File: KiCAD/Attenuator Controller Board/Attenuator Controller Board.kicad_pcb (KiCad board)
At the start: 2 copper layers, 100 x 70 mm, 33 parts, among them J1 Barrel_Jack_Switch, J2 Conn_Coaxial, J3 Conn_Coaxial, J4 Conn_01x24_Female, J5 DSub_15_HD, J6 DSub9, J7 DSub9, J8 DSub9, J9 Conn_01x24_Female, U1 ADM3307EARUZ, U2 ZXMHC3A01T8TA, U3 Teensy3.5

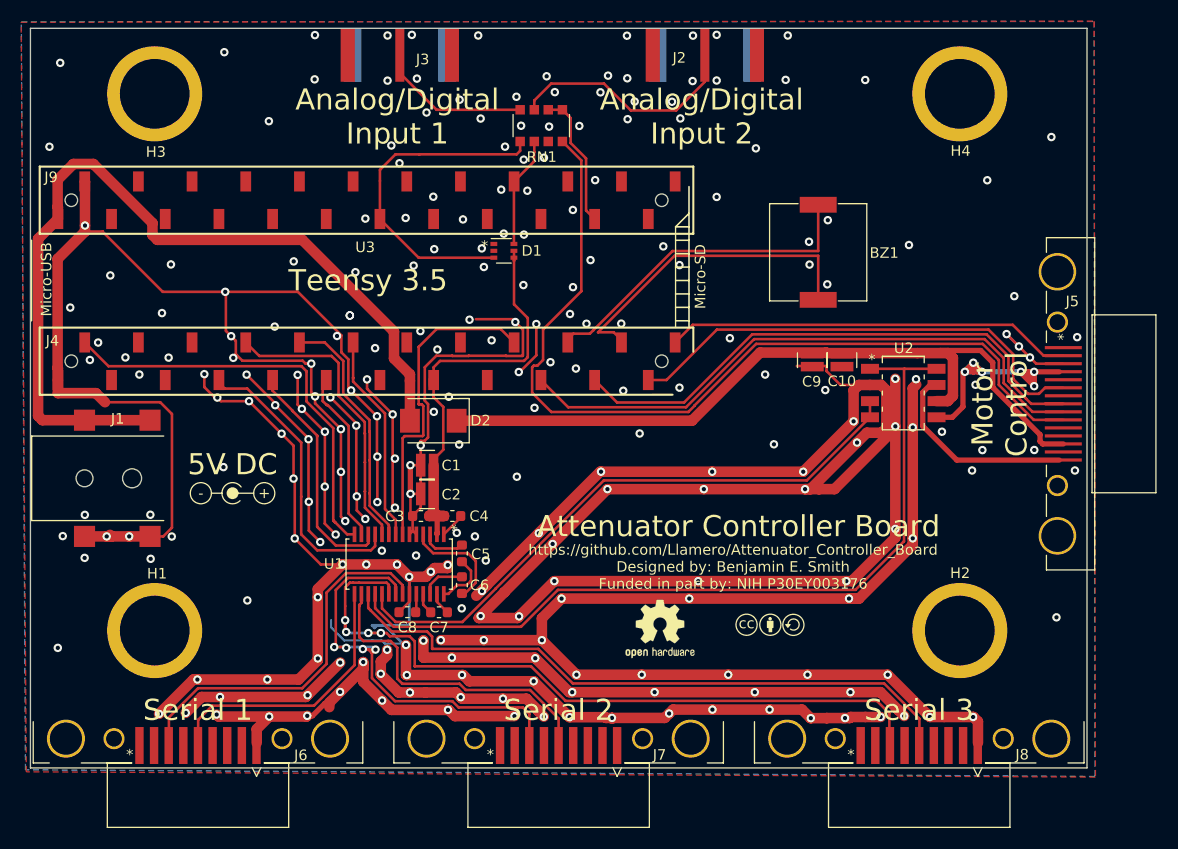
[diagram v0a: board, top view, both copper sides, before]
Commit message: Re-order annotation - add 0.1µF bypass to bypass H-bridge
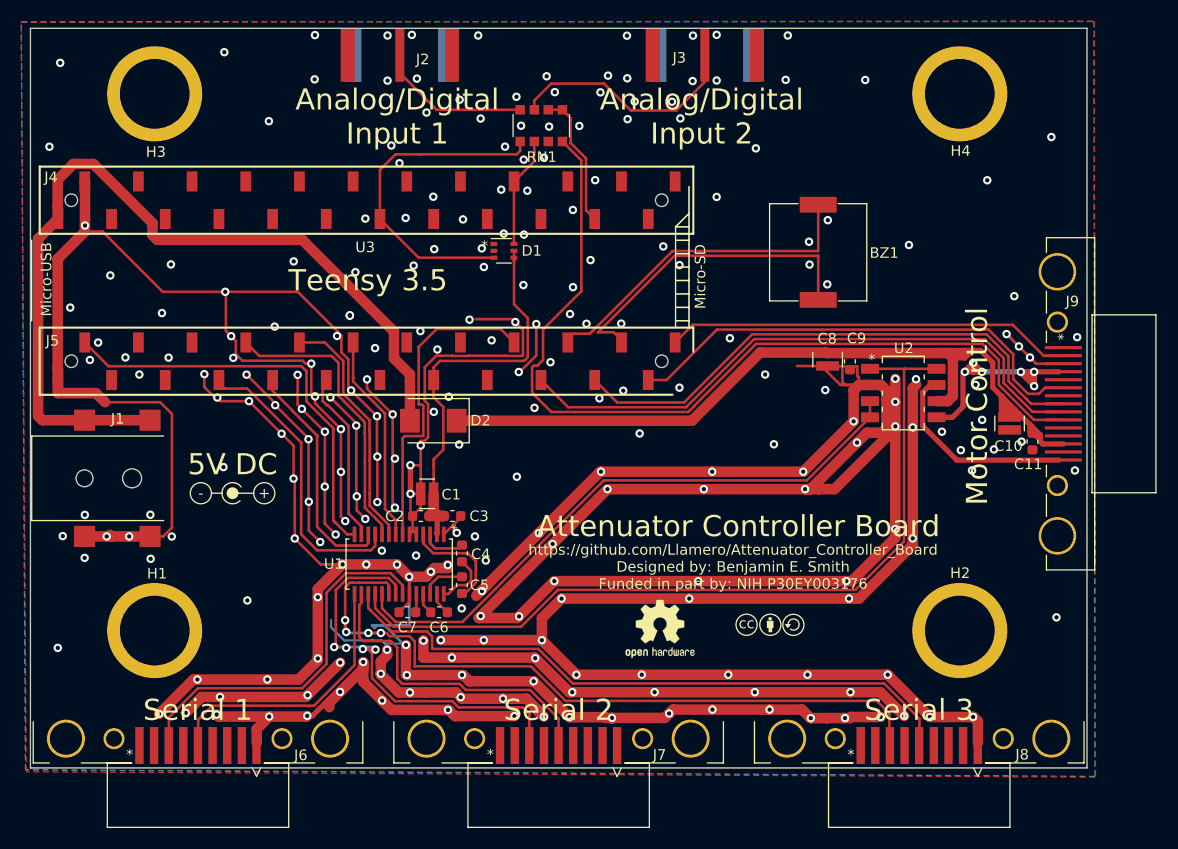
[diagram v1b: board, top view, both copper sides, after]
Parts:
- removed the C1 at (137.6, 111.3)
- added C11: 0.1µF, Capacitor_SMD:C_0603_1608Metric, F.Cu at (194.8, 109.1)
- added C8: 10µF, Custom Footprints:0508_Capacitor, F.Cu at (175.4, 101.3)
- C9: value 10µF -> 0.1µF; footprint Custom Footprints:0508_Capacitor -> Capacitor_SMD:C_0603_1608Metric
- moved C10 19.6 mm to (192.7, 107.4)
- moved C9 0.76 mm to (177.6, 101.5), turned to 90 degrees
- renumbered C2 to C1, C3 to C2, C4 to C3, C5 to C4, C6 to C5, C7 to C6, C8 to C7, J3 to J2, J2 to J3, J9 to J4, J4 to J5, J5 to J9
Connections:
- C9 pad 1: Net-(C10-Pad1) -> GND
- C9 pad 2: GND -> Net-(C10-Pad1)
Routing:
- net Net-(C10-Pad1): track 74.5 -> 86.4 mm
- net GND: track 794.1 -> 801.9 mm, vias 261 -> 264

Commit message: Ground connector housing and standoffs
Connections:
- H1 pad 1: (no net) -> GND
- H2 pad 1: (no net) -> GND
- H3 pad 1: (no net) -> GND
- H4 pad 1: (no net) -> GND
- J6 pad 10: (no net) -> GND
- J7 pad 10: (no net) -> GND
- J8 pad 10: (no net) -> GND
- J9 pad 16: (no net) -> GND

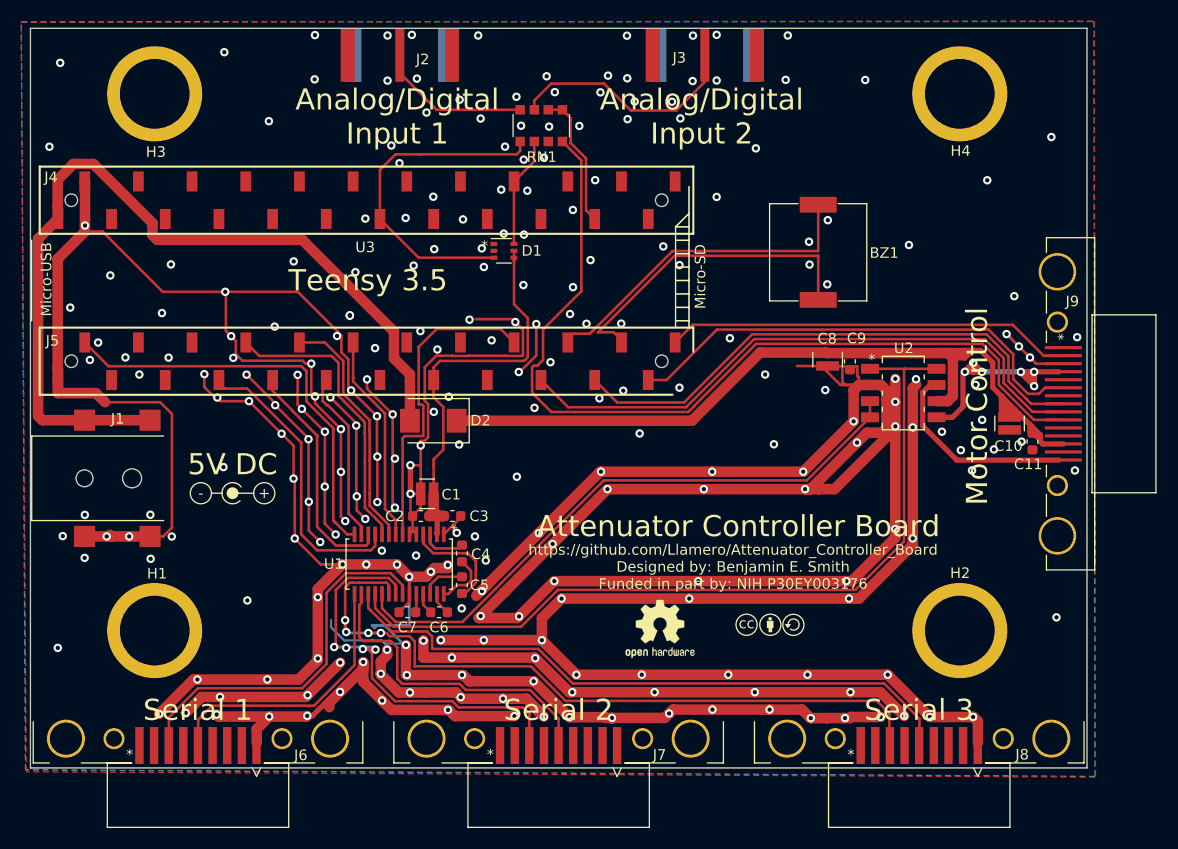
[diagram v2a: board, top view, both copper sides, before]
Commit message: Optional grounding of standoffs - ordered revision
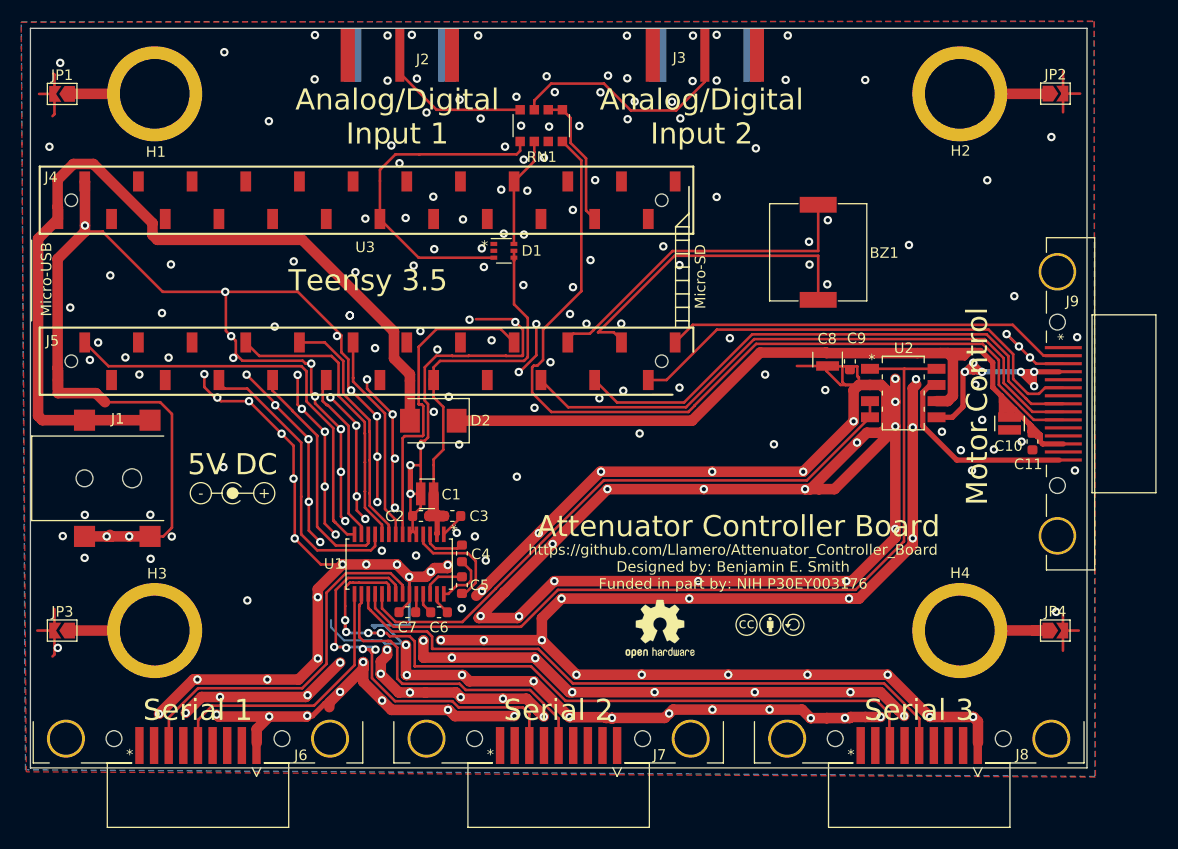
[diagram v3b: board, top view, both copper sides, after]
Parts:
- added JP1: Jumper_NC_Small, Jumper:SolderJumper-2_P1.3mm_Open_TrianglePad1.0x1.5mm, F.Cu at (103.0, 76.2)
- added JP2: Jumper_NC_Small, Jumper:SolderJumper-2_P1.3mm_Open_TrianglePad1.0x1.5mm, F.Cu at (197.0, 76.2)
- added JP3: Jumper_NC_Small, Jumper:SolderJumper-2_P1.3mm_Open_TrianglePad1.0x1.5mm, F.Cu at (103.0, 127.0)
- added JP4: Jumper_NC_Small, Jumper:SolderJumper-2_P1.3mm_Open_TrianglePad1.0x1.5mm, F.Cu at (197.0, 127.0)
- renumbered H3 to H1, H4 to H2, H1 to H3, H2 to H4
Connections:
- H1 pad 1: GND -> Net-(H1-Pad1)
- H2 pad 1: GND -> Net-(H2-Pad1)
- H3 pad 1: GND -> Net-(H3-Pad1)
- H4 pad 1: GND -> Net-(H4-Pad1)
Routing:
- net GND: track 801.9 -> 824.1 mm
- net Net-(H4-Pad1): track 0.00 -> 8.91 mm
- net Net-(H2-Pad1): track 0.00 -> 8.31 mm
- net Net-(H1-Pad1): track 0.00 -> 8.04 mm
- net Net-(H3-Pad1): track 0.00 -> 8.04 mm

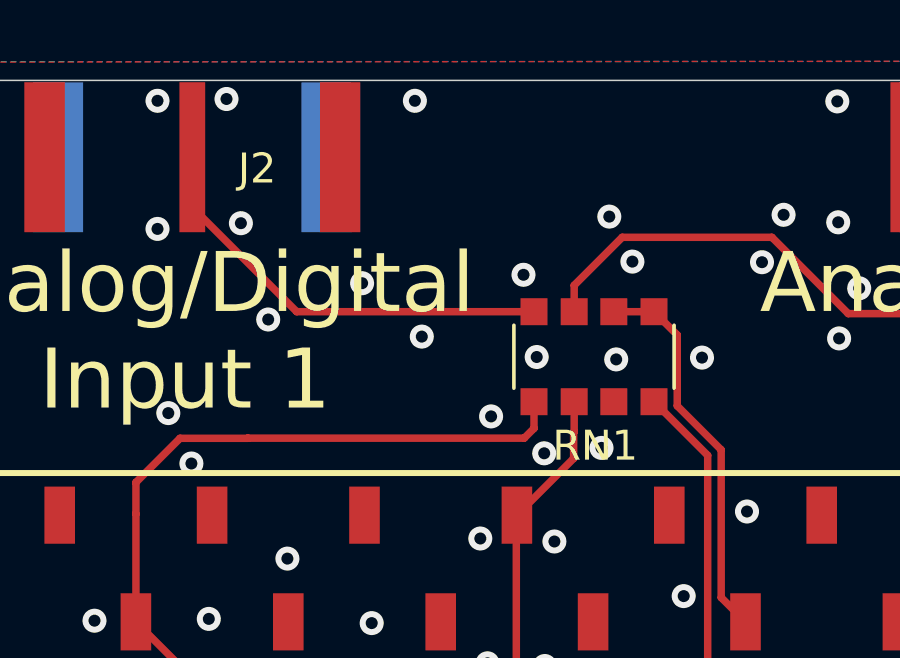
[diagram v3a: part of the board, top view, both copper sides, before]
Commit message: Fixed RN footprint - Test draft of Teensy code
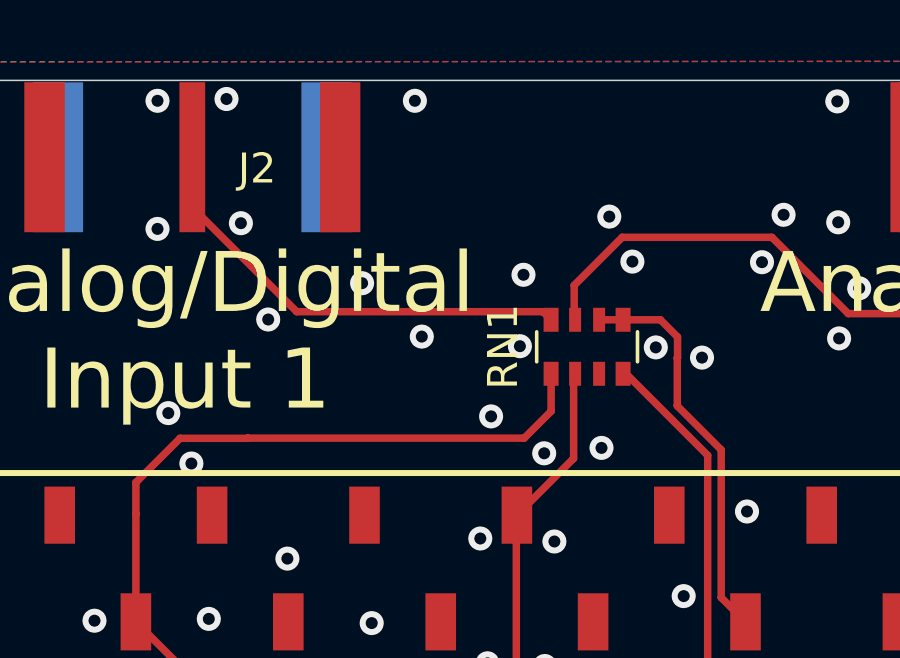
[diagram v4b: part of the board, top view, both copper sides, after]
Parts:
- RN1: footprint Resistor_SMD:R_Array_Convex_4x1206 -> Resistor_SMD:R_Array_Convex_4x0603
- moved RN1 0.40 mm to (148.1, 78.9)
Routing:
- net /Ident_In: track 84.8 -> 86.2 mm
- net /Analog_Input1: track 31.9 -> 33.0 mm
- net /Analog_Input2: track 10.5 -> 11.4 mm
- net Net-(J2-Pad1): track 14.5 -> 15.2 mm
